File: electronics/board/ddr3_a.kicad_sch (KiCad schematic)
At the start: 23 parts, among them U1 DDR3-78

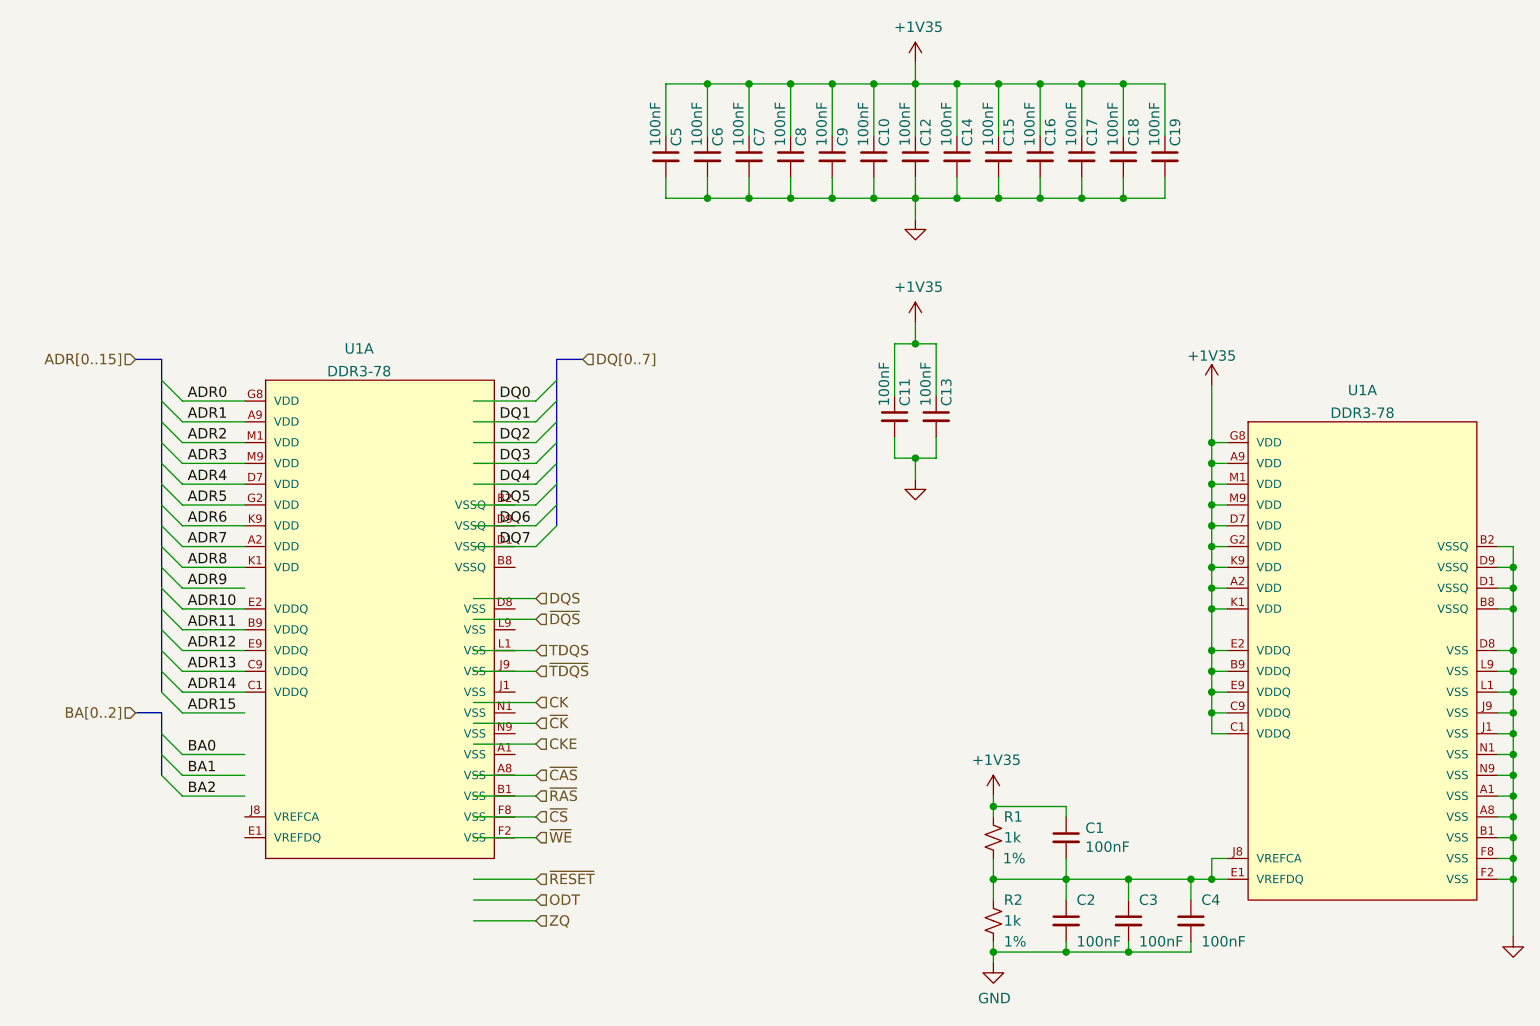
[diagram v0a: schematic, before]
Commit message: Added gitignore, fixed the part
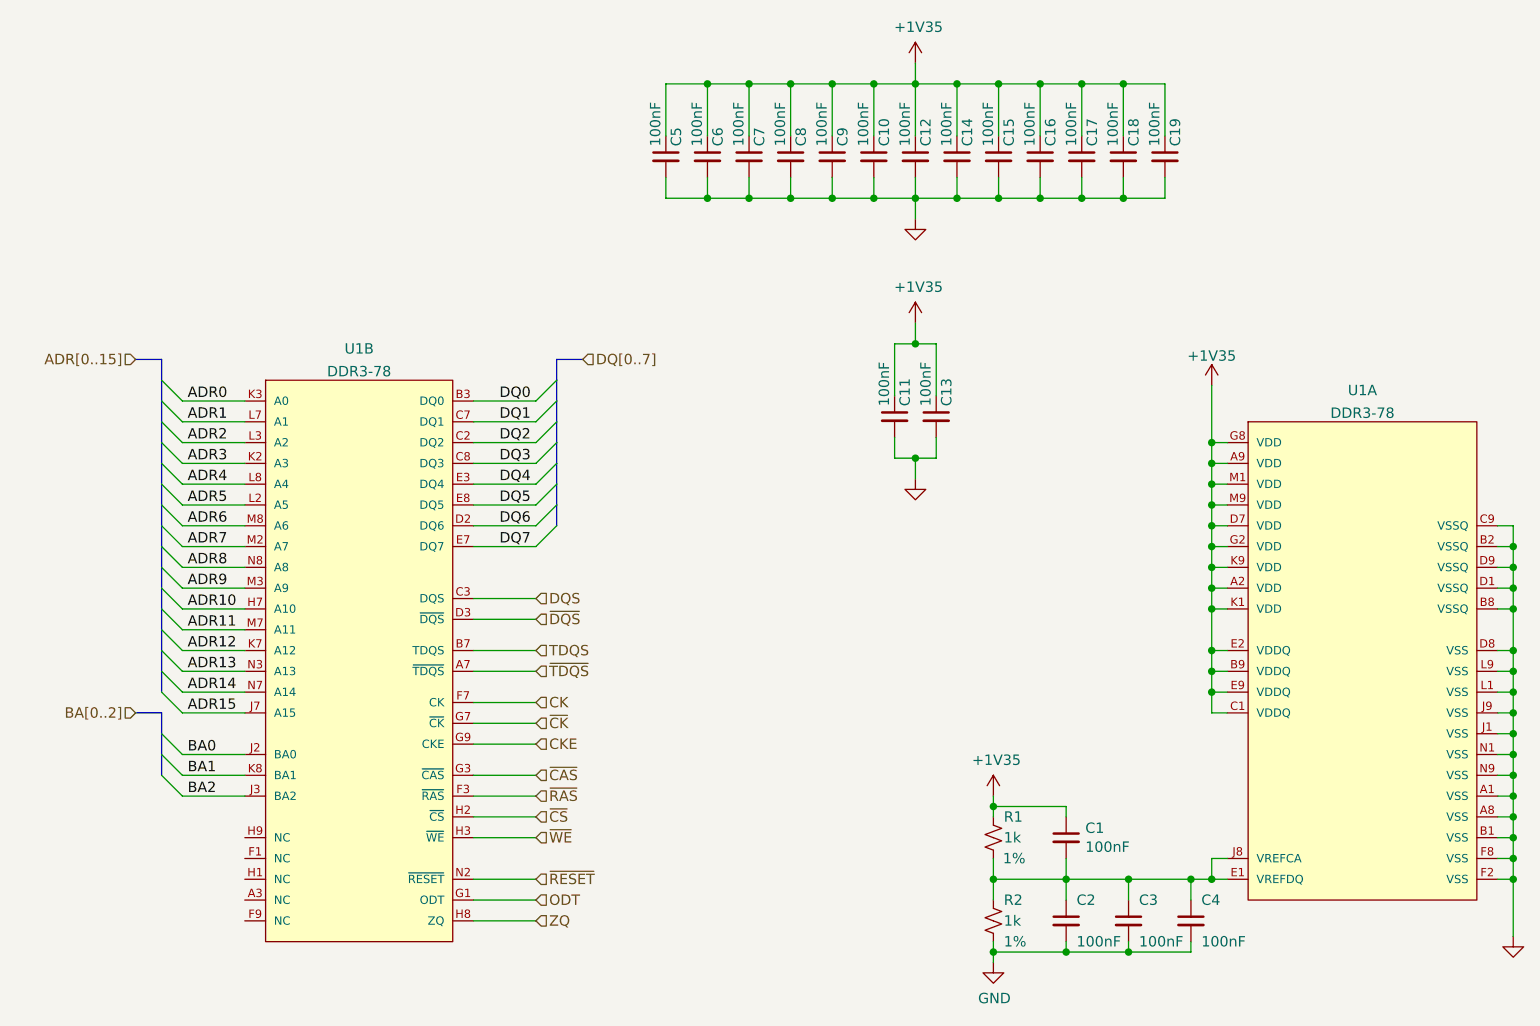
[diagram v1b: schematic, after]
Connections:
- net +1V35: no longer U1.C9 (VDDQ)
- net ADR0: now also U1.K3 (A0); no longer U1.G8 (VDD)
- net ADR1: now also U1.L7 (A1); no longer U1.A9 (VDD)
- net ADR10: now also U1.H7 (A10); no longer U1.E2 (VDDQ)
- net ADR11: now also U1.M7 (A11); no longer U1.B9 (VDDQ)
- net ADR12: now also U1.K7 (A12); no longer U1.E9 (VDDQ)
- net ADR13: now also U1.N3 (A13); no longer U1.C9 (VDDQ)
- net ADR14: now also U1.N7 (A14); no longer U1.C1 (VDDQ)
- net ADR15: now also U1.J7 (A15)
- net ADR2: now also U1.L3 (A2); no longer U1.M1 (VDD)
- net ADR3: now also U1.K2 (A3); no longer U1.M9 (VDD)
- net ADR4: now also U1.L8 (A4); no longer U1.D7 (VDD)
- net ADR5: now also U1.L2 (A5); no longer U1.G2 (VDD)
- net ADR6: now also U1.M8 (A6); no longer U1.K9 (VDD)
- net ADR7: now also U1.M2 (A7); no longer U1.A2 (VDD)
- net ADR8: now also U1.N8 (A8); no longer U1.K1 (VDD)
- net ADR9: now also U1.M3 (A9)
- net BA0: now also U1.J2 (BA0)
- net BA1: now also U1.K8 (BA1)
- net BA2: now also U1.J3 (BA2)
- net CK: now also U1.F7 (CK)
- net CKE: now also U1.G9 (CKE)
- net DQ0: now also U1.B3 (DQ0)
- net DQ1: now also U1.C7 (DQ1)
- net DQ2: now also U1.C2 (DQ2)
- net DQ3: now also U1.C8 (DQ3)
- net DQ4: now also U1.E3 (DQ4)
- net DQ5: now also U1.E8 (DQ5)
- net DQ6: now also U1.D2 (DQ6)
- net DQ7: now also U1.E7 (DQ7)
- net DQS: now also U1.C3 (DQS)
- net GND: now also U1.C9 (VSSQ)
- net ODT: now also U1.G1 (ODT)
- net TDQS: now also U1.B7 (TDQS)
- net ZQ: now also U1.H8 (ZQ)
- net ~{CAS}: now also U1.G3 (~{CAS})
- net ~{CK}: now also U1.G7 (~{CK})
- net ~{CS}: now also U1.H2 (~{CS})
- net ~{DQS}: now also U1.D3 (~{DQS})
- net ~{RAS}: now also U1.F3 (~{RAS})
- net ~{RESET}: now also U1.N2 (~{RESET})
- net ~{TDQS}: now also U1.A7 (~{TDQS})
- net ~{WE}: now also U1.H3 (~{WE})
